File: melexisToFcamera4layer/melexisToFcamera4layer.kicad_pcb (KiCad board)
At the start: 2 copper layers, 56.6 x 57.7 mm, 4 parts

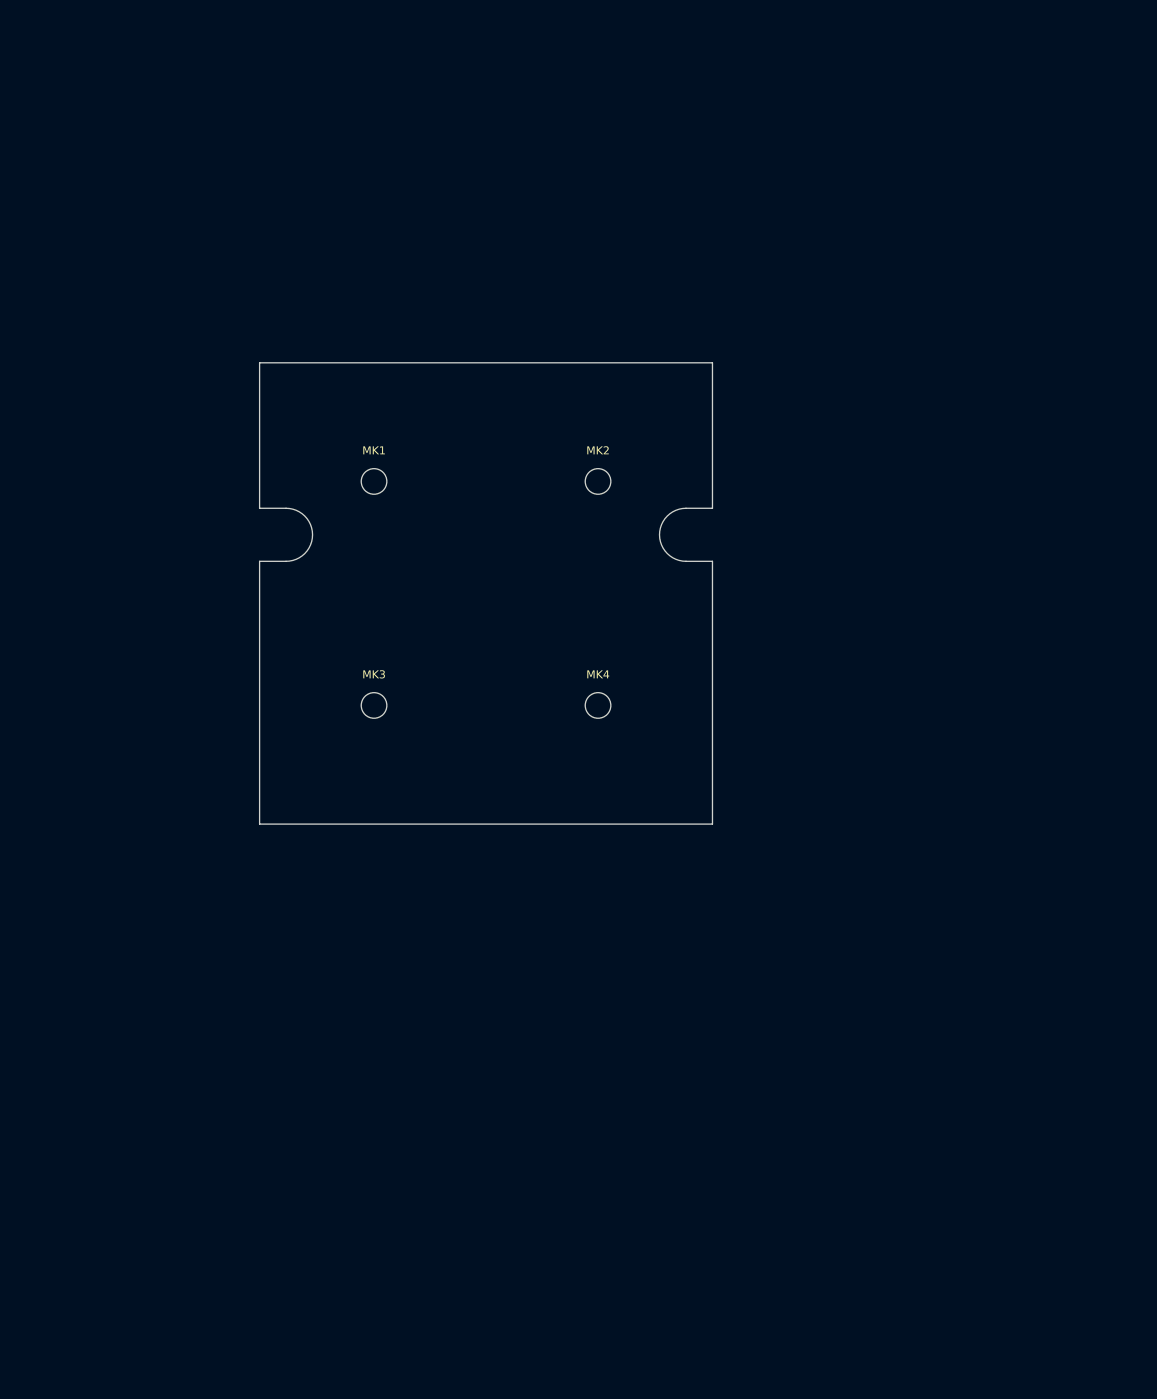
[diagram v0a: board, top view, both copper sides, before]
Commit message: Finalized adding footprints for sensor board, starting routing it.
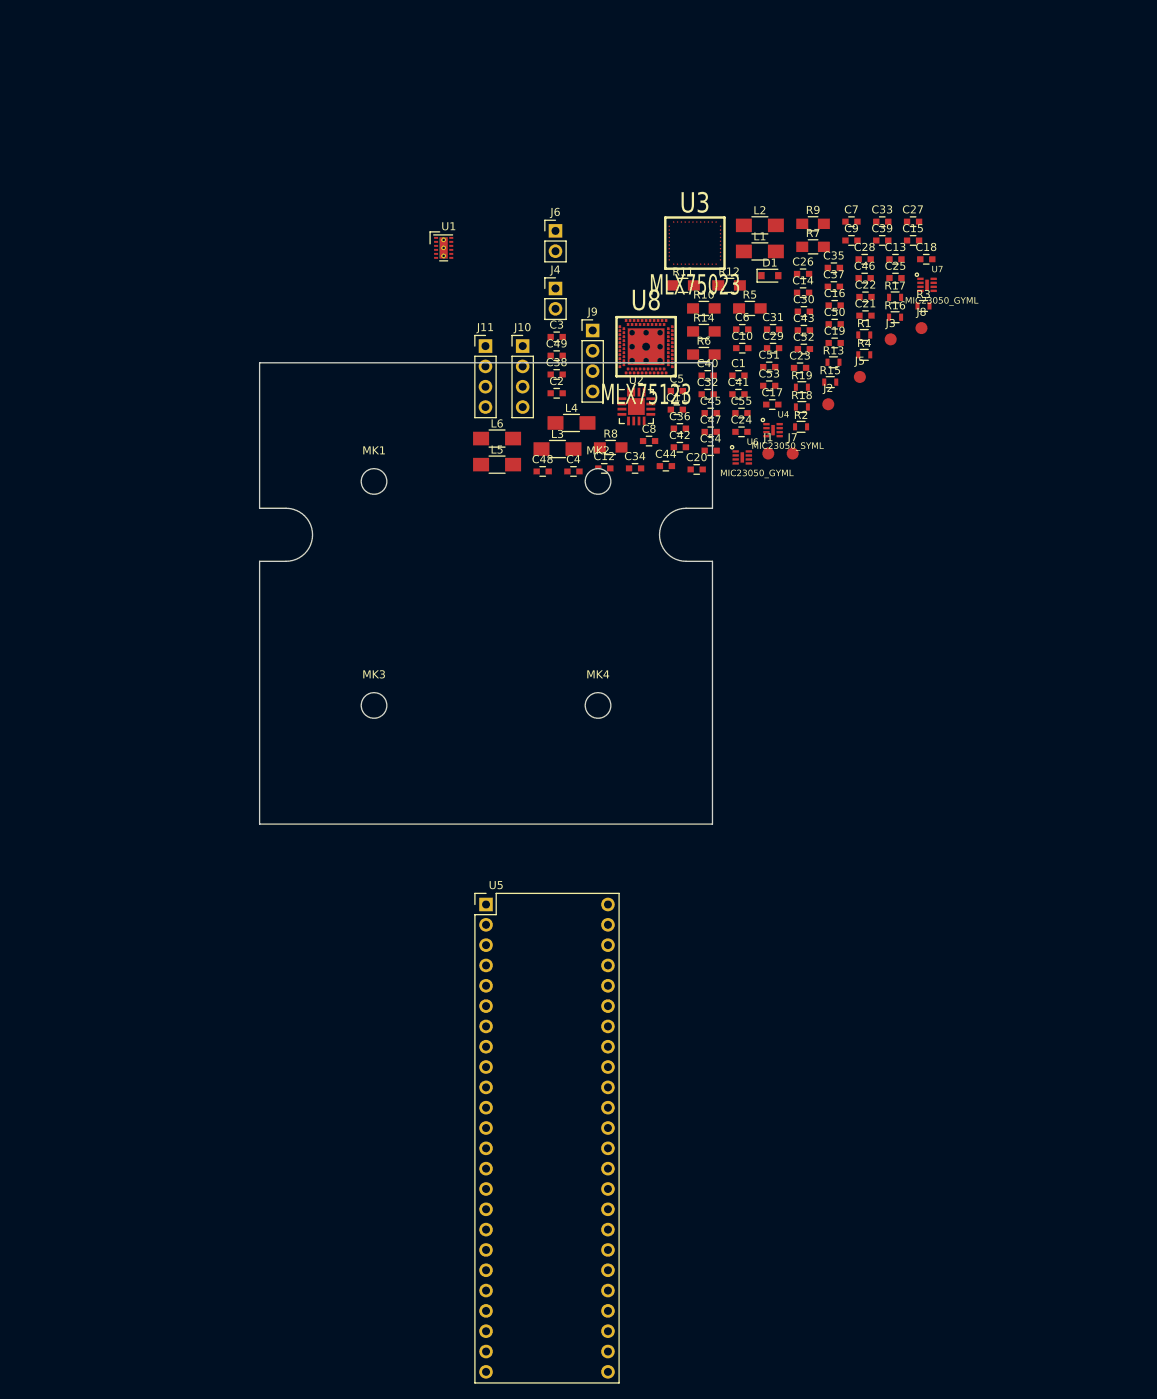
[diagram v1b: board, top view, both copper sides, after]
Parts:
- added C1: 4u7, Capacitors_SMD:C_0603, F.Cu at (133.2, 83.4)
- added C10: 4u7, Capacitors_SMD:C_0603, F.Cu at (133.7, 80.0)
- added C11: 100n, Capacitors_SMD:C_0603, F.Cu at (125.5, 87.7)
- added C12: 1u, Capacitors_SMD:C_0603, F.Cu at (116.5, 95.0)
- added C13: 100n, Capacitors_SMD:C_0603, F.Cu at (152.9, 68.9)
- added C14: 10u, Capacitors_SMD:C_0603, F.Cu at (141.3, 73.0)
- added C15: 100n, Capacitors_SMD:C_0603, F.Cu at (155.1, 66.5)
- added C16: 4u7, Capacitors_SMD:C_0603, F.Cu at (145.3, 74.6)
- added C17: 10u, Capacitors_SMD:C_0603, F.Cu at (137.5, 87.0)
- added C18: 10u, Capacitors_SMD:C_0603, F.Cu at (156.7, 68.9)
- added C19: 4u7, Capacitors_SMD:C_0603, F.Cu at (145.3, 79.3)
- added C2: 10u, Capacitors_SMD:C_0603, F.Cu at (110.5, 85.6)
- added C20: 10u, Capacitors_SMD:C_0603, F.Cu at (128.0, 95.1)
- added C21: 4u7, Capacitors_SMD:C_0603, F.Cu at (149.1, 75.9)
- added C22: 10u, Capacitors_SMD:C_0603, F.Cu at (149.1, 73.6)
- added C23: 2u2, Capacitors_SMD:C_0603, F.Cu at (140.9, 82.4)
- added C24: 2u2, Capacitors_SMD:C_0603, F.Cu at (133.6, 90.4)
- added C25: 4u7, Capacitors_SMD:C_0603, F.Cu at (152.9, 71.2)
- added C26: 100u, Capacitors_SMD:C_0603, F.Cu at (141.3, 70.7)
- added C27: 100n, Capacitors_SMD:C_0603, F.Cu at (155.1, 64.2)
- added C28: 100n, Capacitors_SMD:C_0603, F.Cu at (149.0, 68.9)
- added C29: 10u, Capacitors_SMD:C_0603, F.Cu at (137.6, 80.0)
- added C3: 10u, Capacitors_SMD:C_0603, F.Cu at (110.5, 78.6)
- added C30: 100n, Capacitors_SMD:C_0603, F.Cu at (141.4, 75.4)
- added C31: 10u, Capacitors_SMD:C_0603, F.Cu at (137.6, 77.6)
- added C32: 100n, Capacitors_SMD:C_0603, F.Cu at (129.4, 85.7)
- added C33: 100n, Capacitors_SMD:C_0603, F.Cu at (151.2, 64.2)
- added C34: 100u, Capacitors_SMD:C_0603, F.Cu at (120.3, 95.0)
- added C35: 4u7, Capacitors_SMD:C_0603, F.Cu at (145.2, 69.9)
- added C36: 560p, Capacitors_SMD:C_0603, F.Cu at (125.9, 90.0)
- added C37: 4u7, Capacitors_SMD:C_0603, F.Cu at (145.2, 72.3)
- added C38: 4u7, Capacitors_SMD:C_0603, F.Cu at (110.5, 83.3)
- added C39: 100n, Capacitors_SMD:C_0603, F.Cu at (151.2, 66.5)
- added C4: 100n, Capacitors_SMD:C_0603, F.Cu at (112.6, 95.4)
- added C40: 100n, Capacitors_SMD:C_0603, F.Cu at (129.4, 83.4)
- added C41: 100n, Capacitors_SMD:C_0603, F.Cu at (133.2, 85.7)
- added C42: 560p, Capacitors_SMD:C_0603, F.Cu at (125.9, 92.4)
- added C43: 4u7, Capacitors_SMD:C_0603, F.Cu at (141.4, 77.7)
- added C44: 4u7, Capacitors_SMD:C_0603, F.Cu at (124.2, 94.7)
- added C45: 100n, Capacitors_SMD:C_0603, F.Cu at (129.8, 88.1)
- added C46: 100n, Capacitors_SMD:C_0603, F.Cu at (149.0, 71.2)
- added C47: 100n, Capacitors_SMD:C_0603, F.Cu at (129.8, 90.4)
- added C48: 100n, Capacitors_SMD:C_0603, F.Cu at (108.8, 95.4)
- added C49: 100n, Capacitors_SMD:C_0603, F.Cu at (110.5, 80.9)
- added C5: 4u7, Capacitors_SMD:C_0603, F.Cu at (125.5, 85.3)
- added C50: 100n, Capacitors_SMD:C_0603, F.Cu at (145.3, 77.0)
- added C51: 100n, Capacitors_SMD:C_0603, F.Cu at (137.1, 82.3)
- added C52: 100n, Capacitors_SMD:C_0603, F.Cu at (141.4, 80.1)
- added C53: 560p, Capacitors_SMD:C_0603, F.Cu at (137.1, 84.7)
- added C54: 100n, Capacitors_SMD:C_0603, F.Cu at (129.8, 92.8)
- added C55: 4u7, Capacitors_SMD:C_0603, F.Cu at (133.6, 88.1)
- added C6: 150u, Capacitors_SMD:C_0603, F.Cu at (133.7, 77.6)
- added C7: 10u, Capacitors_SMD:C_0603, F.Cu at (147.4, 64.2)
- added C8: 1u, Capacitors_SMD:C_0603, F.Cu at (122.1, 91.6)
- added C9: 100n, Capacitors_SMD:C_0603, F.Cu at (147.4, 66.5)
- added D1: D, Diodes_SMD:D_0805, F.Cu at (137.2, 70.9)
- added J1: Conn_01x01, Measurement_Points:Measurement_Point_Round-SMD-Pad_Small, F.Cu at (137.0, 93.2)
- added J10: Conn_01x04, Pin_Headers:Pin_Header_Straight_1x04_Pitch2.54mm, F.Cu at (106.3, 79.7)
- added J11: Conn_01x04, Pin_Headers:Pin_Header_Straight_1x04_Pitch2.54mm, F.Cu at (101.6, 79.7)
- added J2: Conn_01x01, Measurement_Points:Measurement_Point_Round-SMD-Pad_Small, F.Cu at (144.5, 87.0)
- added J3: Conn_01x01, Measurement_Points:Measurement_Point_Round-SMD-Pad_Small, F.Cu at (152.3, 78.9)
- added J4: Conn_01x02, Pin_Headers:Pin_Header_Straight_1x02_Pitch2.54mm, F.Cu at (110.4, 72.5)
- added J5: Conn_01x01, Measurement_Points:Measurement_Point_Round-SMD-Pad_Small, F.Cu at (148.4, 83.6)
- added J6: Conn_01x02, Pin_Headers:Pin_Header_Straight_1x02_Pitch2.54mm, F.Cu at (110.4, 65.3)
- added J7: Conn_01x01, Measurement_Points:Measurement_Point_Round-SMD-Pad_Small, F.Cu at (140.0, 93.2)
- added J8: Conn_01x01, Measurement_Points:Measurement_Point_Round-SMD-Pad_Small, F.Cu at (156.1, 77.5)
- added J9: Conn_01x04, Pin_Headers:Pin_Header_Straight_1x04_Pitch2.54mm, F.Cu at (115.0, 77.8)
- added L1: L, Resistors_SMD:R_1206_HandSoldering, F.Cu at (135.9, 67.9)
- added L2: L, Resistors_SMD:R_1206_HandSoldering, F.Cu at (135.9, 64.6)
- added L3: L, Resistors_SMD:R_1206_HandSoldering, F.Cu at (110.6, 92.6)
- added L4: 1u, Resistors_SMD:R_1206_HandSoldering, F.Cu at (112.4, 89.3)
- added L5: 1u, Resistors_SMD:R_1206_HandSoldering, F.Cu at (103.1, 94.5)
- added L6: 1u, Resistors_SMD:R_1206_HandSoldering, F.Cu at (103.1, 91.3)
- added R1: 10k, Resistors_SMD:R_0603, F.Cu at (149.0, 78.3)
- added R10: 316k, Resistors_SMD:R_0805_HandSoldering, F.Cu at (128.9, 75.0)
- added R11: 511k, Resistors_SMD:R_0805_HandSoldering, F.Cu at (126.3, 72.1)
- added R12: 549k, Resistors_SMD:R_0805_HandSoldering, F.Cu at (132.1, 72.1)
- added R13: 10k, Resistors_SMD:R_0603, F.Cu at (145.1, 81.8)
- added R14: 10R, Resistors_SMD:R_0805_HandSoldering, F.Cu at (128.9, 77.9)
- added R15: 10k, Resistors_SMD:R_0603, F.Cu at (144.7, 84.2)
- added R16: 10k, Resistors_SMD:R_0603, F.Cu at (152.8, 76.1)
- added R17: 10k, Resistors_SMD:R_0603, F.Cu at (152.8, 73.6)
- added R18: 10k, Resistors_SMD:R_0603, F.Cu at (141.2, 87.3)
- added R19: 10k, Resistors_SMD:R_0603, F.Cu at (141.2, 84.9)
- added R2: 10k, Resistors_SMD:R_0603, F.Cu at (141.1, 89.8)
- added R3: 10k, Resistors_SMD:R_0603, F.Cu at (156.4, 74.7)
- added R4: 10k, Resistors_SMD:R_0603, F.Cu at (149.0, 80.8)
- added R5: 500, Resistors_SMD:R_0805_HandSoldering, F.Cu at (134.7, 75.0)
- added R6: 27k, Resistors_SMD:R_0805_HandSoldering, F.Cu at (128.9, 80.8)
- added R7: X, Resistors_SMD:R_0805_HandSoldering, F.Cu at (142.6, 67.3)
- added R8: Y, Resistors_SMD:R_0805_HandSoldering, F.Cu at (117.3, 92.4)
- added R9: 953k, Resistors_SMD:R_0805_HandSoldering, F.Cu at (142.6, 64.4)
- added U1: LM27762, footprintsForCamera:LM27762, F.Cu at (96.4, 67.5)
- added U2: ADP2164, footprintsForCamera:ADP2164, F.Cu at (120.5, 87.3)
- added U3: MLX75023, footprintsForCamera:MLX75023, F.Cu at (127.8, 66.9)
- added U4: MIC23050_SYML, footprintsForCamera:MIC23050, F.Cu at (137.6, 90.2)
- added U5: Cmod_A7, footprintsForCamera:Cmod_A7, F.Cu at (101.7, 149.5)
- added U6: MIC23050_GYML, footprintsForCamera:MIC23050, F.Cu at (133.7, 93.6)
- added U7: MIC23050_GYML, footprintsForCamera:MIC23050, F.Cu at (156.8, 72.1)
- added U8: MLX75123, footprintsForCamera:MLX75123, F.Cu at (121.7, 79.8)
- MK1, MK2, MK3, MK4: value Mounting_Hole -> Mounting_Hole_PAD-Mechanical
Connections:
- MK1 pad 1: Net-(MK1-Pad1) -> (no net)
- MK2 pad 1: Net-(MK2-Pad1) -> (no net)
- MK3 pad 1: Net-(MK3-Pad1) -> (no net)
- MK4 pad 1: Net-(MK4-Pad1) -> (no net)

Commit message: Fixed some weird bug in MLX75123 footprint, started routing
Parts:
- moved U3 48.7 mm to (104.0, 109.4)
- moved U8 44.5 mm to (92.8, 113.5)
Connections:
- U8 pad A33: GND -> (no net)
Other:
- copper layers 2 -> 4
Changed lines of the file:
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@@
   )
   (layers
-    (0 F.Cu signal)
-    (31 B.Cu signal)
+    (0 F.Cu power)
+    (1 In1.Cu mixed)
+    (2 In2.Cu mixed)
+    (31 B.Cu mixed)
     (33 F.Adhes user)
     (35 F.Paste user)
     (37 F.SilkS user)
-    (39 F.Mask user)
+    (39 F.Mask user hide)
     (40 Dwgs.User user)
     (41 Cmts.User user)
@@
     (44 Edge.Cuts user)
     (45 Margin user)
+    (46 B.CrtYd user)
     (47 F.CrtYd user)
     (49 F.Fab user)
@@
   )
   (module footprintsForCamera:MLX75123 (layer F.Cu)
-    (at 121.702401 79.802401)
+    (at 92.75 113.55)
     (descr "ToF chipset")
     (tags PGA)
@@
     (pad A32 smd oval (at -2 -3.375 270) (size 0.1 0.3) (layers F.Cu F.Paste F.Mask)
       (net 60 /VSYNC))
-    (pad A33 smd oval (at -2.5 -3.375 270) (size 0.1 0.3) (layers F.Cu F.Paste F.Mask)
-      (net 1 GND) (solder_mask_margin 3))
-    (pad A33 smd oval (at -2.5 -3.175 270) (size 0.1 0.3) (layers F.Cu F.Paste F.Mask)
-      (net 1 GND) (solder_mask_margin 3))
-    (pad A33 smd rect (at -2.5 -3.275 270) (size 0.2 0.3) (layers F.Cu F.Paste F.Mask)
-      (net 1 GND) (solder_mask_margin 3))
     (pad B30 smd rect (at -2.25 -2.775 270) (size 0.2 0.3) (layers F.Cu F.Paste F.Mask)
       (net 5 /DVDD3V3))
@@
     (pad A22 smd oval (at 3.275 -2.4 90) (size 0.1 0.3) (layers F.Cu F.Paste F.Mask)
       (net 1 GND))
+    (pad A33 smd oval (at -2.5 -3.375 270) (size 0.1 0.3) (layers F.Cu F.Paste F.Mask))
+    (pad A33 smd oval (at -2.5 -3.175 270) (size 0.1 0.3) (layers F.Cu F.Paste F.Mask))
+    (pad A33 smd rect (at -2.5 -3.275 270) (size 0.2 0.3) (layers F.Cu F.Paste F.Mask))
   )
   (module footprintsForCamera:MIC23050 (layer F.Cu)
@@
   )
   (module footprintsForCamera:MLX75023 (layer F.Cu)
-    (at 127.802401 66.852401)
+    (at 104.05 109.4)
     (descr "ToF sensor")
     (tags PGA)

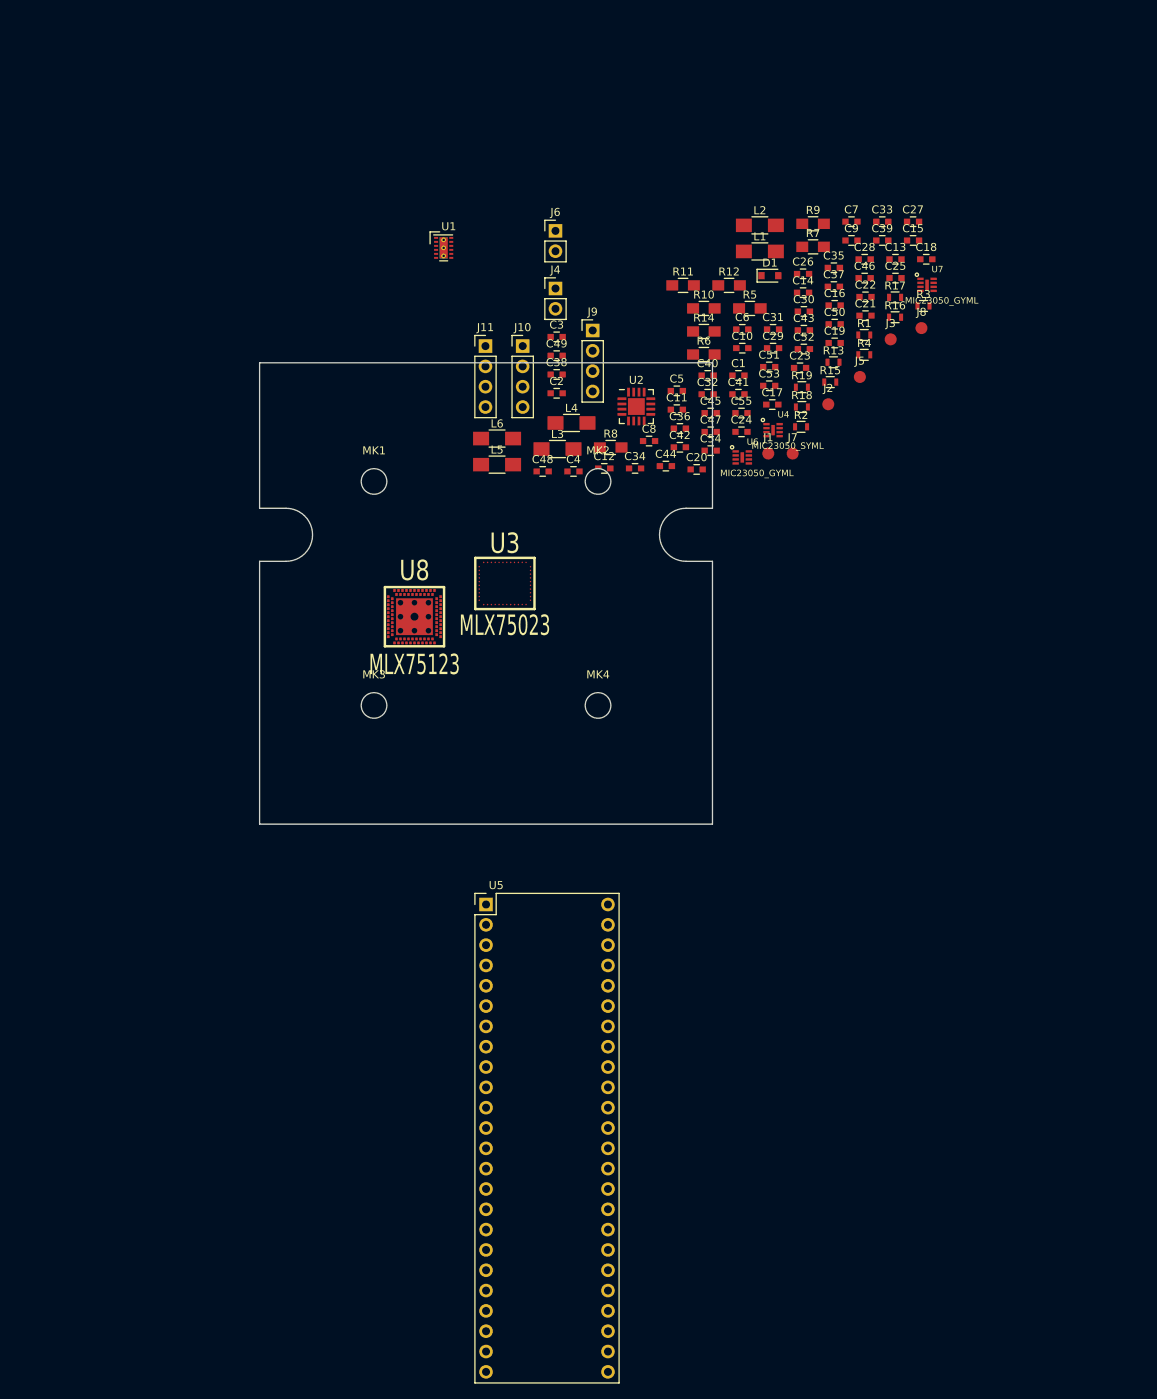
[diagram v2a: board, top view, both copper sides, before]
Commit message: Started placing components on the sensor board
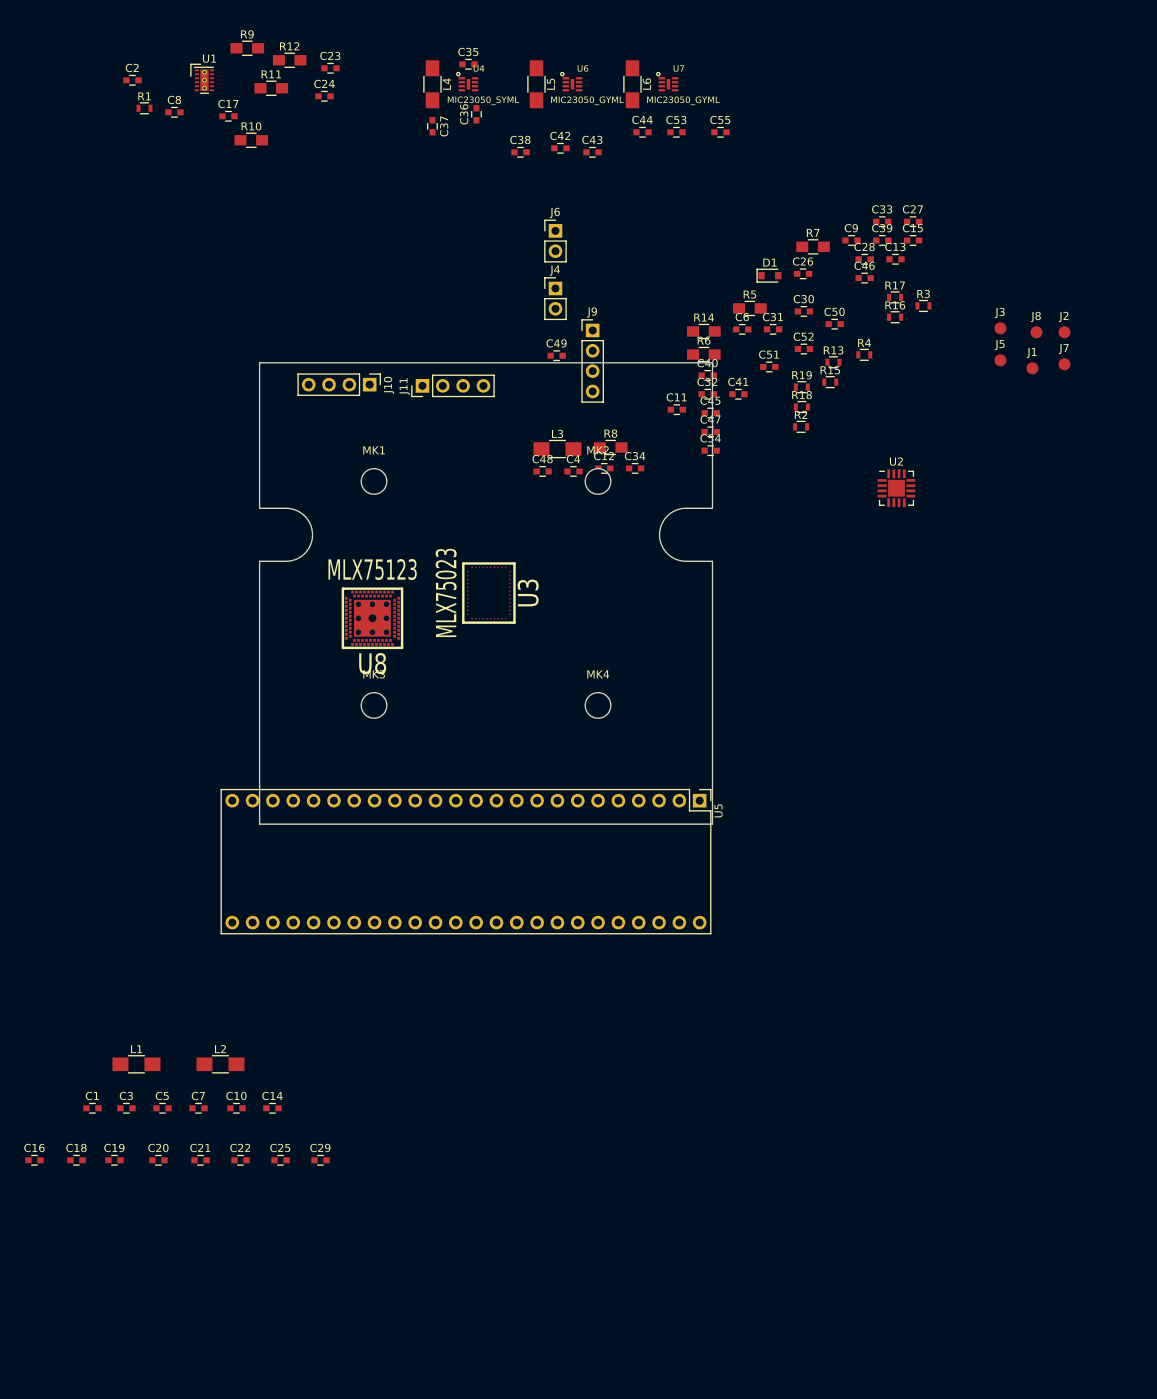
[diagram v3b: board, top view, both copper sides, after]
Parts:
- moved C18 154.8 mm to (50.5, 181.5)
- moved C16 146.4 mm to (45.2, 181.5)
- moved C7 137.6 mm to (65.8, 175.0)
- moved C19 136.2 mm to (55.2, 181.5)
- moved C25 134.4 mm to (76.0, 181.5)
- moved C21 134.4 mm to (66.0, 181.5)
- moved C22 133.2 mm to (71.0, 181.5)
- moved L1 128.0 mm to (58.0, 169.5)
- moved L2 124.7 mm to (68.5, 169.5)
- moved C1 122.1 mm to (52.5, 175.0)
- moved C14 121.6 mm to (75.0, 175.0)
- moved C29 116.2 mm to (81.0, 181.5)
- moved C10 114.1 mm to (70.5, 175.0)
- moved C3 110.4 mm to (56.8, 175.0)
- moved C5 110.3 mm to (61.2, 175.0)
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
